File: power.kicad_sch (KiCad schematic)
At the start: 20 parts, among them U10 TPS562202, U11 AMS1117-3.3

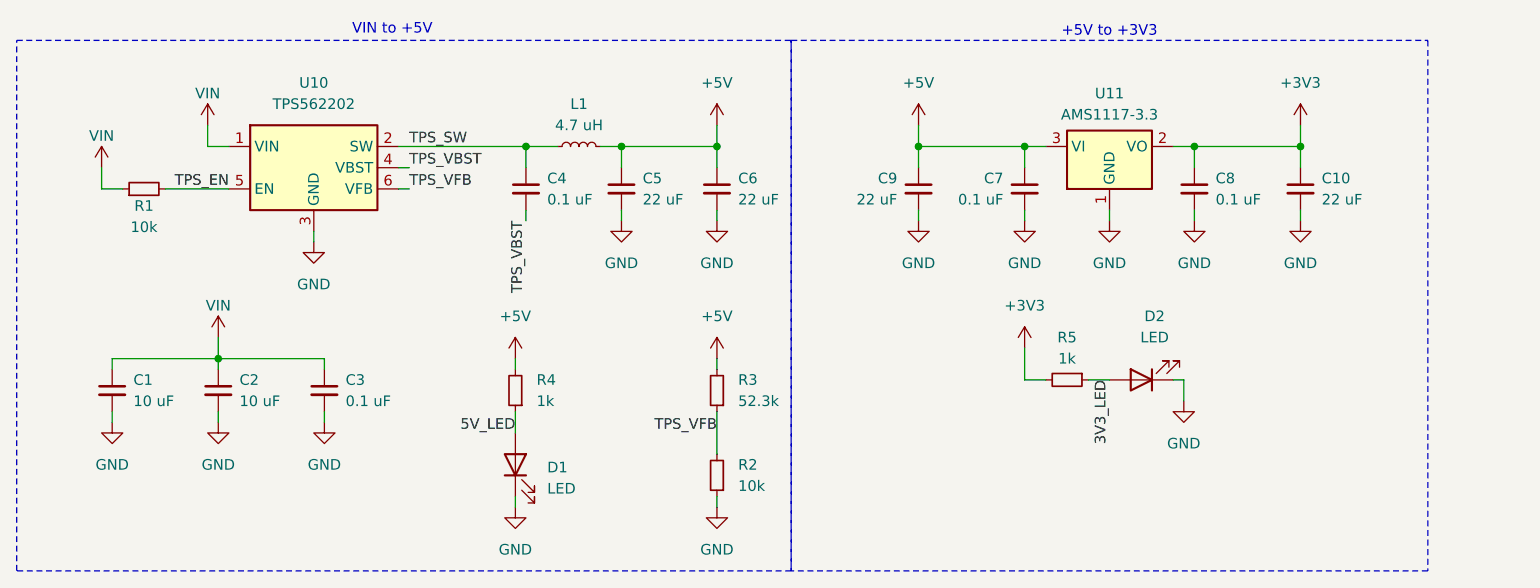
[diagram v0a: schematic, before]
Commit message: Wired barometers and GPS up, added misc LEDs, tidy-up
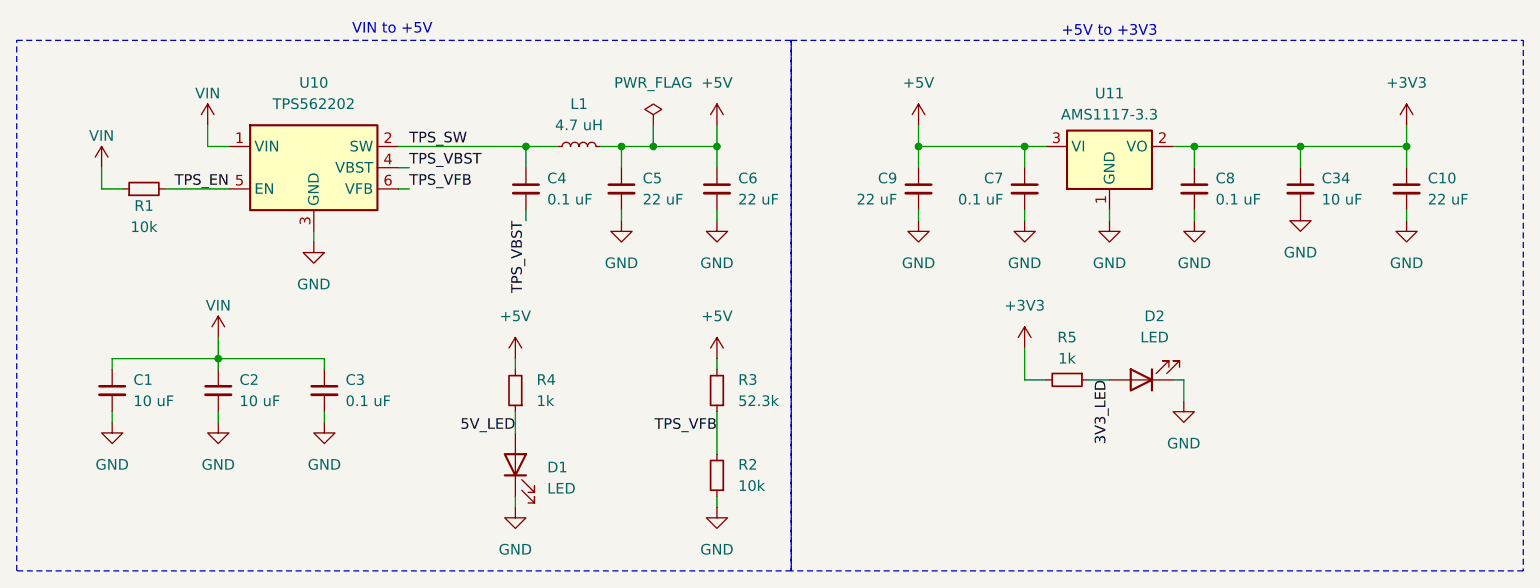
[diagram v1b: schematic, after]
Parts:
- added C34: 10 uF, symbol Device:C_Small
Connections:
- net +3V3: now also C34.1
- net GND: now also C34.2
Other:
- moved on the sheet: C10

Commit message: preliminary schematic wired, all footprints assigned, all laid out in PCB editor.
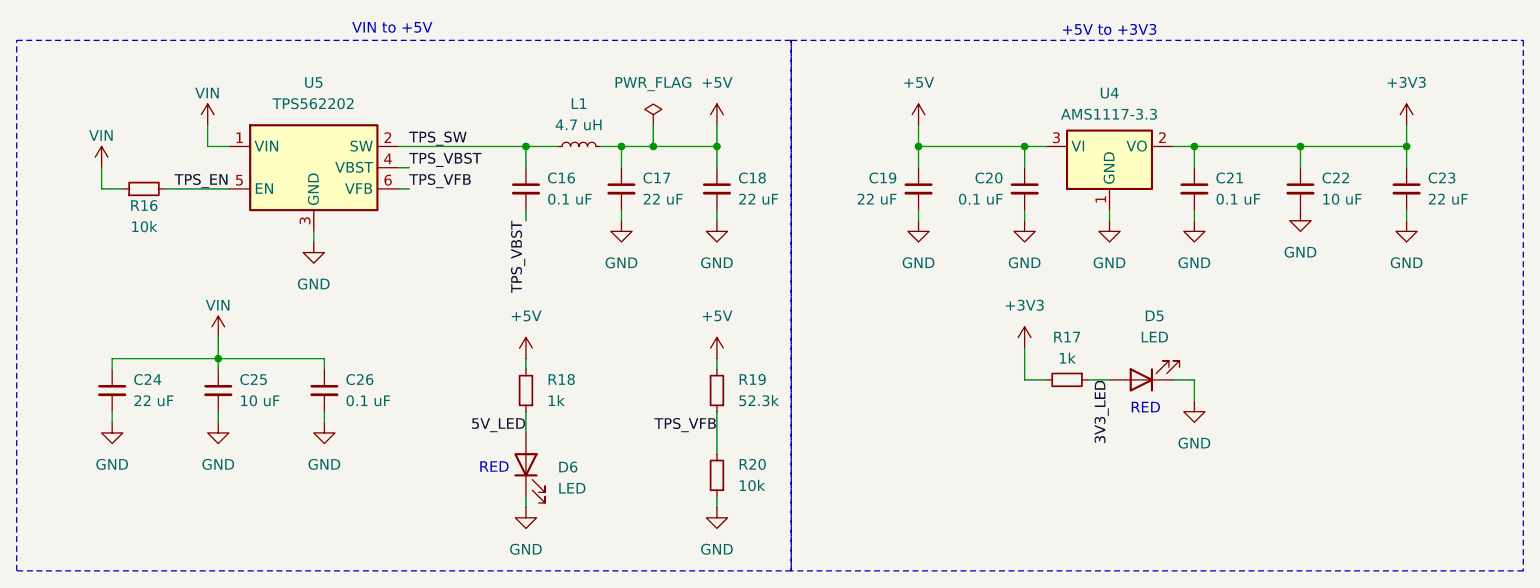
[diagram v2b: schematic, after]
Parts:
- removed C1: 10 uF, Capacitor_SMD:C_0805_2012Metric, symbol Device:C_Small
- added C24: 22 uF, Capacitor_SMD:C_0805_2012Metric, symbol Device:C_Small
- C17: renamed from C5; footprint Capacitor_SMD:C_0805_2012Metric -> Capacitor_SMD:C_0201_0603Metric
- C18: renamed from C6; footprint Capacitor_SMD:C_0805_2012Metric -> Capacitor_SMD:C_0201_0603Metric
- C19: renamed from C9; footprint (none) -> Capacitor_SMD:C_0603_1608Metric
- C22: renamed from C34; footprint (none) -> Capacitor_SMD:C_0603_1608Metric
- C23: renamed from C10; footprint (none) -> Capacitor_SMD:C_0603_1608Metric
- L1: footprint Inductor_SMD:L_6.3x6.3_H3 -> SparkFun-Capacitor:C_0805_2012Metric
- R16: renamed from R1; footprint (none) -> Resistor_SMD:R_0603_1608Metric
- R17: renamed from R5; footprint (none) -> Resistor_SMD:R_0603_1608Metric
- R18: renamed from R4; footprint (none) -> Resistor_SMD:R_0603_1608Metric
- R19: renamed from R3; footprint (none) -> Resistor_SMD:R_0603_1608Metric
- R20: renamed from R2; footprint (none) -> Resistor_SMD:R_0603_1608Metric
- renumbered C4 to C16, C7 to C20, C8 to C21, C2 to C25, C3 to C26, D2 to D5, D1 to D6, U11 to U4, U10 to U5
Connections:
- net GND: now also C24.2
- net VIN: now also C24.1
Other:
- note added: "RED"
- moved on the sheet: D6, R18

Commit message: reassigned some footprints, preliminary PCB layout
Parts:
- C16, C20, C21: footprint Capacitor_SMD:C_0805_2012Metric -> Capacitor_SMD:C_0603_1608Metric
- C17, C18: footprint Capacitor_SMD:C_0201_0603Metric -> Capacitor_SMD:C_0603_1608Metric
- D5, D6: footprint LED_SMD:LED_0805_2012Metric -> LED_SMD:LED_0603_1608Metric
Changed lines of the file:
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@@
 			)
 		)
-		(property "Footprint" "LED_SMD:LED_0805_2012Metric"
+		(property "Footprint" "LED_SMD:LED_0603_1608Metric"
 			(at 111.76 109.22 0)
 			(effects
@@
 			)
 		)
-		(property "Footprint" "Capacitor_SMD:C_0201_0603Metric"
+		(property "Footprint" "Capacitor_SMD:C_0603_1608Metric"
 			(at 123.19 76.2 0)
 			(effects
@@
 			)
 		)
-		(property "Footprint" "Capacitor_SMD:C_0201_0603Metric"
+		(property "Footprint" "Capacitor_SMD:C_0603_1608Metric"
 			(at 134.62 76.2 0)
 			(effects
@@
 			)
 		)
-		(property "Footprint" "Capacitor_SMD:C_0805_2012Metric"
+		(property "Footprint" "Capacitor_SMD:C_0603_1608Metric"
 			(at 111.76 76.2 0)
 			(effects
@@
 			)
 		)
-		(property "Footprint" "Capacitor_SMD:C_0805_2012Metric"
+		(property "Footprint" "Capacitor_SMD:C_0603_1608Metric"
 			(at 191.77 76.2 0)
 			(effects
@@
 			)
 		)
-		(property "Footprint" "Capacitor_SMD:C_0805_2012Metric"
+		(property "Footprint" "Capacitor_SMD:C_0603_1608Metric"
 			(at 171.45 76.2 0)
 			(effects
@@
 			)
 		)
-		(property "Footprint" "LED_SMD:LED_0805_2012Metric"
+		(property "Footprint" "LED_SMD:LED_0603_1608Metric"
 			(at 185.42 99.06 0)
 			(effects

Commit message: added missing output diodes, added 3d models, misc. re-laying
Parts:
- L1: footprint SparkFun-Capacitor:C_0805_2012Metric -> Valkyrie_footprints:HPC 5020NF
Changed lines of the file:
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@@
 			)
 		)
-		(property "Footprint" "SparkFun-Capacitor:C_0805_2012Metric"
+		(property "Footprint" "Valkyrie_footprints:HPC 5020NF"
 			(at 118.11 78.74 0)
 			(effects

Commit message: did some clean-up, did some to-do tasks.
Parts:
- renumbered D5 to D6, D6 to D7
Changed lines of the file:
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@@
 		(dnp no)
 		(fields_autoplaced yes)
-		(property "Reference" "#PWR056"
+		(property "Reference" "#PWR057"
 			(at 111.76 100.33 0)
 			(effects
@@
 			(project "valkyriev3"
 				(path "/d24fd15c-a242-4d26-9876-7755ca0d378c/739f0b15-c53d-4f01-9ae2-b7e797c20069"
-					(reference "#PWR056")
+					(reference "#PWR057")
 					(unit 1)
 				)
@@
 		(dnp no)
 		(fields_autoplaced yes)
-		(property "Reference" "D6"
+		(property "Reference" "D7"
 			(at 115.57 109.5374 90)
 			(effects
@@
 			(project ""
 				(path "/d24fd15c-a242-4d26-9876-7755ca0d378c/739f0b15-c53d-4f01-9ae2-b7e797c20069"
-					(reference "D6")
+					(reference "D7")
 					(unit 1)
 				)
@@
 		(dnp no)
 		(fields_autoplaced yes)
-		(property "Reference" "#PWR044"
+		(property "Reference" "#PWR045"
 			(at 60.96 77.47 0)
 			(effects
@@
 			(project "valkyriev3"
 				(path "/d24fd15c-a242-4d26-9876-7755ca0d378c/739f0b15-c53d-4f01-9ae2-b7e797c20069"
-					(reference "#PWR044")
+					(reference "#PWR045")
 					(unit 1)
 				)
@@
 		(dnp no)
 		(fields_autoplaced yes)
-		(property "Reference" "#PWR050"
+		(property "Reference" "#PWR051"
 			(at 181.61 86.36 0)
 			(effects
@@
 			(project "valkyriev3"
 				(path "/d24fd15c-a242-4d26-9876-7755ca0d378c/739f0b15-c53d-4f01-9ae2-b7e797c20069"
-					(reference "#PWR050")
+					(reference "#PWR051")
 					(unit 1)
 				)
@@
 		(dnp no)
 		(fields_autoplaced yes)
-		(property "Reference" "#PWR051"
+		(property "Reference" "#PWR052"
 			(at 191.77 86.36 0)
 			(effects
@@
 			(project "valkyriev3"
 				(path "/d24fd15c-a242-4d26-9876-7755ca0d378c/739f0b15-c53d-4f01-9ae2-b7e797c20069"
-					(reference "#PWR051")
+					(reference "#PWR052")
 					(unit 1)
 				)
@@
 		(dnp no)
 		(fields_autoplaced yes)
-		(property "Reference" "#PWR047"
+		(property "Reference" "#PWR048"
 			(at 134.62 86.36 0)
 			(effects
@@
 			(project "valkyriev3"
 				(path "/d24fd15c-a242-4d26-9876-7755ca0d378c/739f0b15-c53d-4f01-9ae2-b7e797c20069"
-					(reference "#PWR047")
+					(reference "#PWR048")
 					(unit 1)
 				)
@@
 		(dnp no)
 		(fields_autoplaced yes)
-		(property "Reference" "#PWR062"
+		(property "Reference" "#PWR063"
 			(at 111.76 120.65 0)
 			(effects
@@
 			(project "valkyriev3"
 				(path "/d24fd15c-a242-4d26-9876-7755ca0d378c/739f0b15-c53d-4f01-9ae2-b7e797c20069"
-					(reference "#PWR062")
+					(reference "#PWR063")
 					(unit 1)
 				)
@@
 		(dnp no)
 		(fields_autoplaced yes)
-		(property "Reference" "#PWR060"
+		(property "Reference" "#PWR061"
 			(at 74.93 110.49 0)
 			(effects
@@
 			(project "valkyriev3"
 				(path "/d24fd15c-a242-4d26-9876-7755ca0d378c/739f0b15-c53d-4f01-9ae2-b7e797c20069"
-					(reference "#PWR060")
+					(reference "#PWR061")
 					(unit 1)
 				)
@@
 		(dnp no)
 		(fields_autoplaced yes)
-		(property "Reference" "#PWR061"
+		(property "Reference" "#PWR062"
 			(at 87.63 110.49 0)
 			(effects
@@
 			(project "valkyriev3"
 				(path "/d24fd15c-a242-4d26-9876-7755ca0d378c/739f0b15-c53d-4f01-9ae2-b7e797c20069"
-					(reference "#PWR061")
+					(reference "#PWR062")
 					(unit 1)
 				)
@@
 		(dnp no)
 		(fields_autoplaced yes)
-		(property "Reference" "#PWR043"
+		(property "Reference" "#PWR044"
 			(at 217.17 72.39 0)
 			(effects
@@
 			(project ""
 				(path "/d24fd15c-a242-4d26-9876-7755ca0d378c/739f0b15-c53d-4f01-9ae2-b7e797c20069"
-					(reference "#PWR043")
+					(reference "#PWR044")
 					(unit 1)
 				)
@@
 		(dnp no)
 		(fields_autoplaced yes)
-		(property "Reference" "#PWR048"
+		(property "Reference" "#PWR049"
 			(at 158.75 86.36 0)
 			(effects
@@
 			(project "valkyriev3"
 				(path "/d24fd15c-a242-4d26-9876-7755ca0d378c/739f0b15-c53d-4f01-9ae2-b7e797c20069"
-					(reference "#PWR048")
+					(reference "#PWR049")
 					(unit 1)
 				)
@@
 		(dnp no)
 		(fields_autoplaced yes)
-		(property "Reference" "#PWR040"
+		(property "Reference" "#PWR041"
 			(at 73.66 72.39 0)
 			(effects
@@
 			(project "valkyriev3"
 				(path "/d24fd15c-a242-4d26-9876-7755ca0d378c/739f0b15-c53d-4f01-9ae2-b7e797c20069"
-					(reference "#PWR040")
+					(reference "#PWR041")
 					(unit 1)
 				)
@@
 		(dnp no)
 		(fields_autoplaced yes)
-		(property "Reference" "#PWR045"
+		(property "Reference" "#PWR046"
 			(at 204.47 85.09 0)
 			(effects
@@
 			(project "valkyriev3"
 				(path "/d24fd15c-a242-4d26-9876-7755ca0d378c/739f0b15-c53d-4f01-9ae2-b7e797c20069"
-					(reference "#PWR045")
+					(reference "#PWR046")
 					(unit 1)
 				)
@@
 		(dnp no)
 		(fields_autoplaced yes)
-		(property "Reference" "#PWR058"
+		(property "Reference" "#PWR059"
 			(at 191.77 107.95 0)
 			(effects
@@
 			(project "valkyriev3"
 				(path "/d24fd15c-a242-4d26-9876-7755ca0d378c/739f0b15-c53d-4f01-9ae2-b7e797c20069"
-					(reference "#PWR058")
+					(reference "#PWR059")
 					(unit 1)
 				)
@@
 		(dnp no)
 		(fields_autoplaced yes)
-		(property "Reference" "#PWR054"
+		(property "Reference" "#PWR055"
 			(at 74.93 97.79 0)
 			(effects
@@
 			(project ""
 				(path "/d24fd15c-a242-4d26-9876-7755ca0d378c/739f0b15-c53d-4f01-9ae2-b7e797c20069"
-					(reference "#PWR054")
+					(reference "#PWR055")
 					(unit 1)
 				)
@@
 		(dnp no)
 		(fields_autoplaced yes)
-		(property "Reference" "#PWR063"
+		(property "Reference" "#PWR064"
 			(at 134.62 120.65 0)
 			(effects
@@
 			(project "valkyriev3"
 				(path "/d24fd15c-a242-4d26-9876-7755ca0d378c/739f0b15-c53d-4f01-9ae2-b7e797c20069"
-					(reference "#PWR063")
+					(reference "#PWR064")
 					(unit 1)
 				)
@@
 		(dnp no)
 		(fields_autoplaced yes)
-		(property "Reference" "#PWR052"
+		(property "Reference" "#PWR053"
 			(at 217.17 86.36 0)
 			(effects
@@
 			(project "valkyriev3"
 				(path "/d24fd15c-a242-4d26-9876-7755ca0d378c/739f0b15-c53d-4f01-9ae2-b7e797c20069"
-					(reference "#PWR052")
+					(reference "#PWR053")
 					(unit 1)
 				)
@@
 		(dnp no)
 		(fields_autoplaced yes)
-		(property "Reference" "#PWR041"
+		(property "Reference" "#PWR042"
 			(at 134.62 72.39 0)
 			(effects
@@
 			(project ""
 				(path "/d24fd15c-a242-4d26-9876-7755ca0d378c/739f0b15-c53d-4f01-9ae2-b7e797c20069"
-					(reference "#PWR041")
+					(reference "#PWR042")
 					(unit 1)
 				)
@@
 		(dnp no)
 		(fields_autoplaced yes)
-		(property "Reference" "#PWR046"
+		(property "Reference" "#PWR047"
 			(at 123.19 86.36 0)
 			(effects
@@
 			(project "valkyriev3"
 				(path "/d24fd15c-a242-4d26-9876-7755ca0d378c/739f0b15-c53d-4f01-9ae2-b7e797c20069"
-					(reference "#PWR046")
+					(reference "#PWR047")
 					(unit 1)
 				)
@@
 		(dnp no)
 		(fields_autoplaced yes)
-		(property "Reference" "#PWR057"
+		(property "Reference" "#PWR058"
 			(at 134.62 100.33 0)
 			(effects
@@
 			(project "valkyriev3"
 				(path "/d24fd15c-a242-4d26-9876-7755ca0d378c/739f0b15-c53d-4f01-9ae2-b7e797c20069"
-					(reference "#PWR057")
+					(reference "#PWR058")
 					(unit 1)
 				)
@@
 		(dnp no)
 		(fields_autoplaced yes)
-		(property "Reference" "#PWR053"
+		(property "Reference" "#PWR054"
 			(at 86.36 88.9 0)
 			(effects
@@
 			(project "valkyriev3"
 				(path "/d24fd15c-a242-4d26-9876-7755ca0d378c/739f0b15-c53d-4f01-9ae2-b7e797c20069"
-					(reference "#PWR053")
+					(reference "#PWR054")
 					(unit 1)
 				)
@@
 		(dnp no)
 		(fields_autoplaced yes)
-		(property "Reference" "#PWR055"
+		(property "Reference" "#PWR056"
 			(at 171.45 99.06 0)
 			(effects
@@
 			(project "valkyriev3"
 				(path "/d24fd15c-a242-4d26-9876-7755ca0d378c/739f0b15-c53d-4f01-9ae2-b7e797c20069"
-					(reference "#PWR055")
+					(reference "#PWR056")
 					(unit 1)
 				)
@@
 		(dnp no)
 		(fields_autoplaced yes)
-		(property "Reference" "#PWR059"
+		(property "Reference" "#PWR060"
 			(at 62.23 110.49 0)
 			(effects
@@
 			(project ""
 				(path "/d24fd15c-a242-4d26-9876-7755ca0d378c/739f0b15-c53d-4f01-9ae2-b7e797c20069"
-					(reference "#PWR059")
+					(reference "#PWR060")
 					(unit 1)
 				)
@@
 		(dnp no)
 		(fields_autoplaced yes)
-		(property "Reference" "#PWR042"
+		(property "Reference" "#PWR043"
 			(at 158.75 72.39 0)
 			(effects
@@
 			(project "valkyriev3"
 				(path "/d24fd15c-a242-4d26-9876-7755ca0d378c/739f0b15-c53d-4f01-9ae2-b7e797c20069"
-					(reference "#PWR042")
+					(reference "#PWR043")
 					(unit 1)
 				)
@@
 		(dnp no)
 		(fields_autoplaced yes)
-		(property "Reference" "#PWR049"
+		(property "Reference" "#PWR050"
 			(at 171.45 86.36 0)
 			(effects
@@
 			(project "valkyriev3"
 				(path "/d24fd15c-a242-4d26-9876-7755ca0d378c/739f0b15-c53d-4f01-9ae2-b7e797c20069"
-					(reference "#PWR049")
+					(reference "#PWR050")
 					(unit 1)
 				)
@@
 		(dnp no)
 		(fields_autoplaced yes)
-		(property "Reference" "D5"
+		(property "Reference" "D6"
 			(at 187.0075 91.44 0)
 			(effects
@@
 			(project "valkyriev3"
 				(path "/d24fd15c-a242-4d26-9876-7755ca0d378c/739f0b15-c53d-4f01-9ae2-b7e797c20069"
-					(reference "D5")
+					(reference "D6")
 					(unit 1)
 				)
